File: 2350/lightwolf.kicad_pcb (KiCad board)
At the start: 4 copper layers, 21 x 51 mm, 52 parts, among them Q1 XC6220B331MR-G, U1 DS1021-1X20SF11-B, U2 W25Q32JVSNIQ, U3 DS1021-1X20SF11-B, U4 RP2350A_C42411118, U5 ABM8-272-T3_C20625731, U6 0603L100SLYR

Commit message: feat: update design files and add production files
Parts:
- C12: renamed from C3; value 4.7uF -> 10uF
- renumbered C4 to C1, C19 to C10, C20 to C11, C9 to C13, C12 to C14, C14 to C15, C2 to C16, C5 to C17, C11 to C18, C7 to C19, C6 to C2, C8 to C3, C10 to C4, C13 to C5, C15 to C6, C16 to C7, C17 to C8, C1 to C9, H3 to H2, H2 to H3, R8 to R1, R11 to R10, R12 to R11, R13 to R12, R4 to R13, R10 to R4, R9 to R5, R5 to R6, R6 to R7, R1 to R8, R7 to R9, U5 to U1, U6 to U2, U2 to U3, U1 to U5, U3 to U6

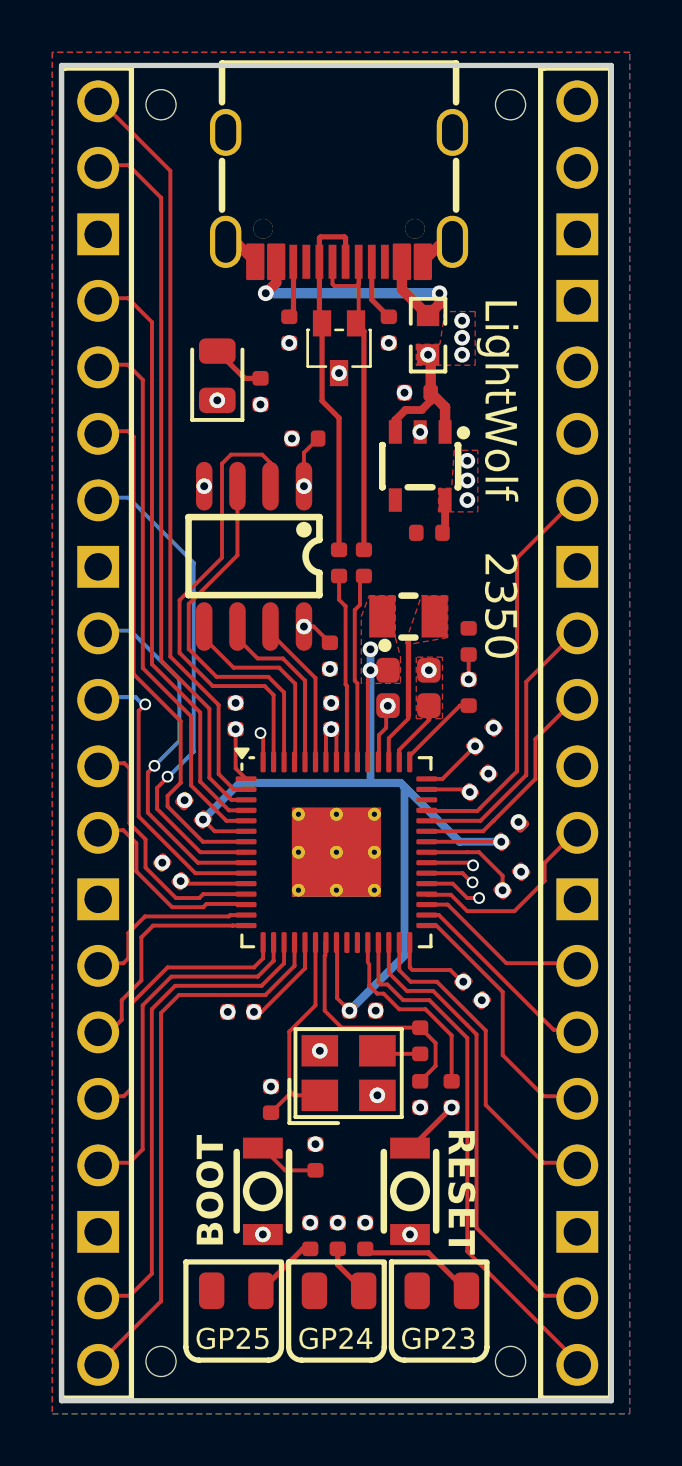
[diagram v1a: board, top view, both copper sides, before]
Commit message: fix: design issue and update project files
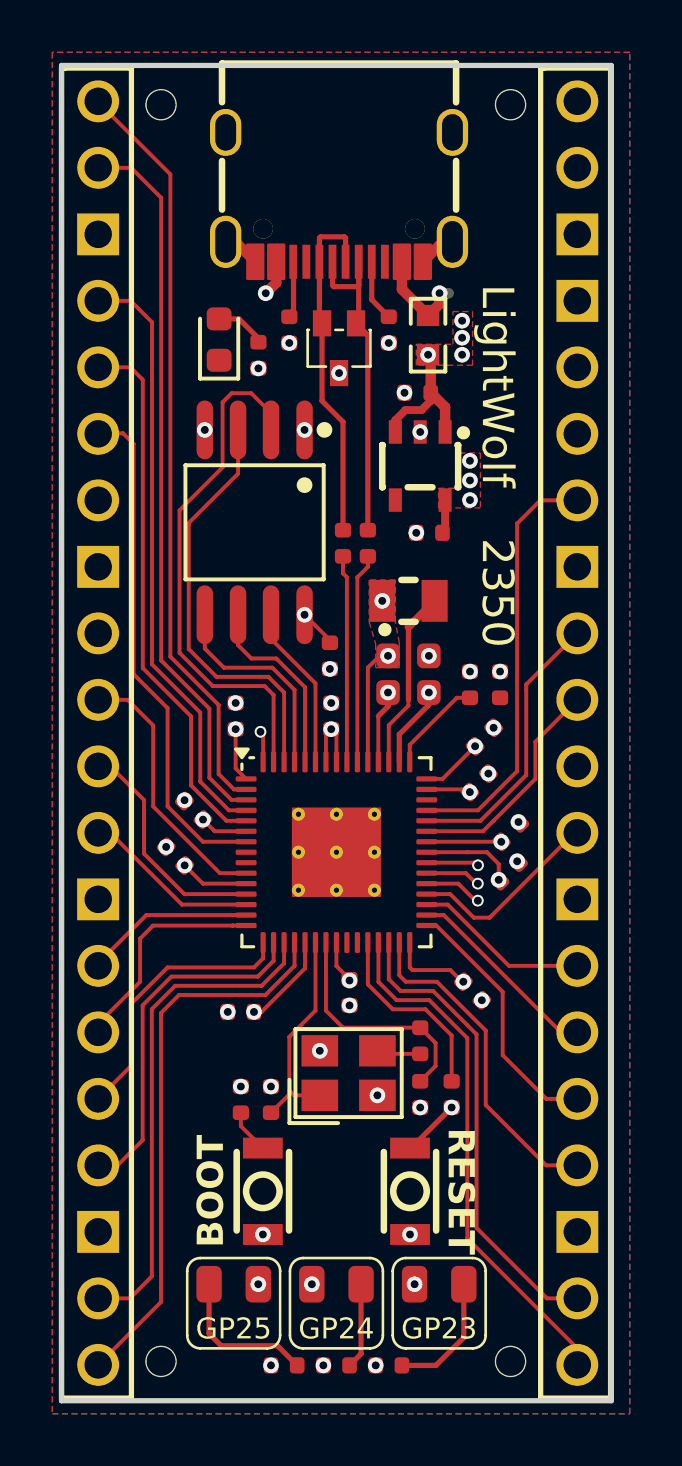
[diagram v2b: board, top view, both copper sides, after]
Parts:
- removed R5: 0Ω, PCM_JLCPCB:R_0402
- added G***: LOGO, LOGO, B.Cu at (146.4, 113.7)
- C1: value 100nF -> 470nF
- D2: footprint PCM_JLCPCB:D_0805 -> PCM_JLCPCB:D_0603
- U3: value W25Q32JVSNIQ -> W25Q64JVSSIQ_C179171; footprint easyeda2kicad:SOP-8_L4.9-W3.9-P1.27-LS6.0-BL -> easyeda2kicad:SOIC-8_L5.3-W5.3-P1.27-LS8.0-BL
- moved R10 5.05 mm to (144.4, 120.2), turned to 180 degrees
- moved R12 5.03 mm to (148.4, 120.2), turned to 180 degrees
- moved R11 4.95 mm to (146.4, 120.2), turned to 180 degrees
- moved R8 3.60 mm to (142.8, 110.0)
- moved C19 2.04 mm to (152.7, 94.2), turned to -90 degrees
- moved R4 1.38 mm to (143.4, 81.6)
- moved D2 1.38 mm to (141.9, 81.0)
- moved U3 1.30 mm to (143.3, 88.0)
- moved C14 0.86 mm to (146.9, 105.9), turned to -90 degrees
- moved R6 0.76 mm to (146.7, 88.8)
- moved R7 0.76 mm to (147.6, 88.8)
- moved C3 0.62 mm to (140.2, 100.7)
- moved L1 0.60 mm to (149.2, 91.0)
- moved C18 0.55 mm to (149.2, 93.0)
- moved C17 0.50 mm to (149.2, 94.5)
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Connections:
- D3 pad 1: GND -> Net-(U4-GPIO25)
- D4 pad 1: GND -> Net-(U4-GPIO24)
- D5 pad 1: GND -> Net-(U4-GPIO23)
- R10 pad 1: Net-(U4-GPIO25) -> Net-(D3-Pad2)
- R10 pad 2: Net-(D3-Pad2) -> +3V3
- R11 pad 1: Net-(U4-GPIO24) -> Net-(D4-Pad2)
- R11 pad 2: Net-(D4-Pad2) -> +3V3
- R12 pad 1: Net-(U4-GPIO23) -> Net-(D5-Pad2)
- R12 pad 2: Net-(D5-Pad2) -> +3V3
- U4 pad 8: /GP5 -> unconnected-(U4-GPIO5-Pad8)
- U4 pad 9: /GP6 -> unconnected-(U4-GPIO6-Pad9)
- U5 pad 12: /GP6 -> +5V
- U5 pad 14: /GP5 -> +3V3
- U6 pad 20: +5V -> USBVBUS
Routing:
- net /GP5: track 18.8 -> 0.00 mm, vias 1 -> 0
- net /GP6: track 14.0 -> 0.00 mm, vias 1 -> 0
- net USBVBUS: track 11.5 -> 21.8 mm
- net Net-(U4-GPIO25): track 19.2 -> 26.7 mm
- net Net-(U4-GPIO24): track 17.9 -> 25.1 mm
- net GND: track 11.3 -> 6.10 mm, vias 26 -> 27
- net +3V3: track 32.1 -> 27.6 mm, vias 16 -> 19
- net Net-(U4-GPIO23): track 17.2 -> 20.8 mm
- net Net-(D3-Pad2): track 2.55 -> 5.75 mm
- net /QSPI_SS: track 29.9 -> 27.6 mm
- net /QSPI_SP1: track 17.7 -> 20.0 mm
- net /QSPI_SP2: track 14.0 -> 16.1 mm
- net Net-(U4-VREG_LX): track 5.13 -> 6.87 mm
- net Net-(D4-Pad2): track 2.01 -> 3.28 mm
- net /GP28: track 15.6 -> 16.8 mm
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- removed copper zone on F.Cu, net Net-(U4-VREG_LX)
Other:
- board text added: "4 MB"
- board text added: "VBUS"
- board text removed: "GP5"
- board text removed: "GP6"
- board text removed: "v1.0"

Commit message: fix: decoupling issue for VREG_AVDD
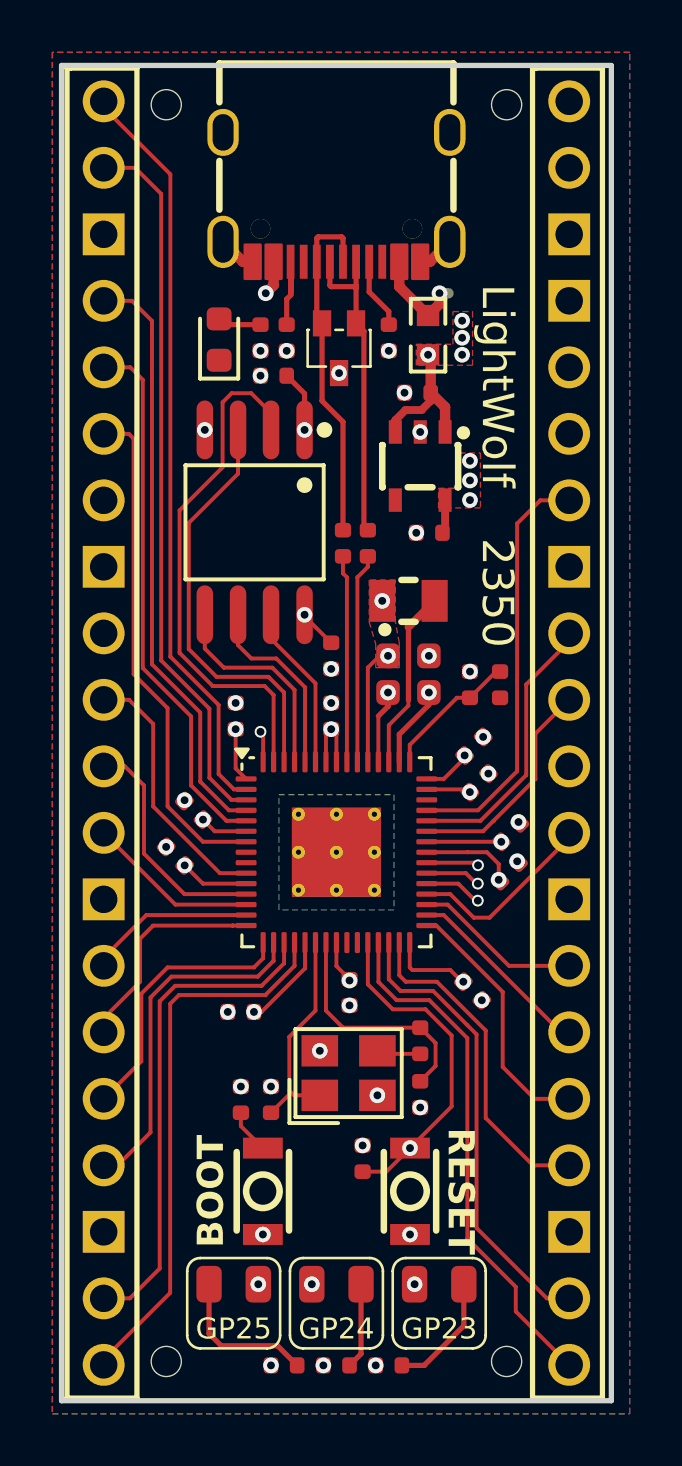
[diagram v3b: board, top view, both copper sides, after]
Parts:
- added R5: 10kΩ, PCM_JLCPCB:R_0402, F.Cu at (144.0, 82.3)
- R13: value 5.1kΩ -> 10kΩ
- moved G*** 18.5 mm to (146.4, 95.2)
- moved R13 4.19 mm to (147.4, 112.2), turned to 90 degrees
- moved R4 0.67 mm to (143.5, 80.9)
- moved C8 0.53 mm to (151.7, 96.5)
- moved R2 0.32 mm to (144.5, 80.9)
- moved U6 0.31 mm to (155.3, 96.0)
- moved R3 0.30 mm to (148.4, 80.9)
- moved U5 0.21 mm to (137.5, 96.0)
- moved H1 0.20 mm to (139.9, 72.0)
- moved H2 0.20 mm to (139.9, 120.0)
- moved H3 0.15 mm to (152.9, 72.0)
- moved H4 0.15 mm to (152.9, 120.0)
- moved USBC1 0.10 mm to (146.4, 75.5)
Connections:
- C19 pad 1: +3V3 -> Net-(U4-VREG_AVDD)
- R13 pad 1: Net-(U4-RUN) -> /RUN
- R13 pad 2: /RUN -> +3V3
- U4 pad 26: Net-(U4-RUN) -> /RUN
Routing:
- net /RUN: track 18.8 -> 31.1 mm
- net +1V1: track 38.0 -> 48.3 mm
- net Net-(U4-RUN): track 7.36 -> 0.00 mm
- net /QSPI_SS: track 27.6 -> 30.0 mm
- net Net-(U4-VREG_AVDD): track 3.70 -> 5.26 mm
- net Net-(USBC1-CC2): track 2.17 -> 3.20 mm
- net Net-(U4-GPIO24): track 25.1 -> 24.3 mm
- net /USBDN: track 13.2 -> 12.5 mm
- net /GP8: track 8.90 -> 9.48 mm
- net /GP16: track 20.0 -> 20.5 mm
- net +3V3: track 27.6 -> 27.1 mm, vias 19 -> 20
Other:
- board text added: "wolf-yuan.dev"
